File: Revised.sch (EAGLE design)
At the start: 17 parts, among them IC1 ATMEGA328P_PDIP

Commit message: Small tweaks
Remove capacitive coupling to RST#, which should enable debugWIRE
Thicken the power and ground traces, tweaking routes for clearance
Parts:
- removed C3: 0.1uF, SparkFun-Capacitors:CAP0402-CAP
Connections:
- removed net N$3: C3.2, IC1.PC6(/RESET), R1.1
- net RTS#: now also IC1.PC6(/RESET), R1.1; no longer C3.1
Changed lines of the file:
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@@
 <class number="0" name="default" width="0" drill="0">
 </class>
-<class number="1" name="power" width="0.6096" drill="0">
+<class number="1" name="power" width="0.8128" drill="0">
 </class>
 </classes>
@@
 <part name="R_TX" library="rcl" deviceset="R-US_" device="R0805" value="1k"/>
 <part name="R_RX" library="rcl" deviceset="R-US_" device="R0805" value="1k"/>
-<part name="C3" library="SparkFun-Capacitors" deviceset="CAP" device="0402-CAP" value="0.1uF"/>
 <part name="C1" library="rcl" deviceset="CPOL-US" device="E2,5-6E" value="47uF"/>
 <part name="JP1" library="jumper" deviceset="JP2E" device=""/>
@@
 <instance part="R_TX" gate="G$1" x="22.86" y="53.34"/>
 <instance part="R_RX" gate="G$1" x="22.86" y="60.96"/>
-<instance part="C3" gate="G$1" x="53.34" y="91.44" rot="R180"/>
 <instance part="C1" gate="G$1" x="2.54" y="101.6"/>
 <instance part="JP1" gate="1" x="20.32" y="91.44" rot="R180"/>
@@
 </segment>
 </net>
-<net name="N$3" class="0">
-<segment>
-<pinref part="C3" gate="G$1" pin="2"/>
-<wire x1="53.34" y1="99.06" x2="53.34" y2="93.98" width="0.1524" layer="91"/>
-<wire x1="53.34" y1="99.06" x2="58.42" y2="99.06" width="0.1524" layer="91"/>
-<label x="53.34" y="99.06" size="1.778" layer="95"/>
-<pinref part="R1" gate="G$1" pin="1"/>
-<wire x1="48.26" y1="99.06" x2="53.34" y2="99.06" width="0.1524" layer="91"/>
-<junction x="53.34" y="99.06"/>
-</segment>
-<segment>
-<pinref part="IC1" gate="G$1" pin="PC6(/RESET)"/>
-<wire x1="86.36" y1="93.98" x2="76.2" y2="93.98" width="0.1524" layer="91"/>
-<label x="76.2" y="93.98" size="1.778" layer="95"/>
-</segment>
-</net>
 <net name="TXD" class="0">
 <segment>
@@
 </segment>
 <segment>
-<pinref part="C3" gate="G$1" pin="1"/>
-<wire x1="53.34" y1="86.36" x2="53.34" y2="73.66" width="0.1524" layer="91"/>
-<label x="53.34" y="73.66" size="1.778" layer="95" rot="R90"/>
-</segment>
-</net>
+<label x="53.34" y="99.06" size="1.778" layer="95"/>
+<pinref part="R1" gate="G$1" pin="1"/>
+<wire x1="48.26" y1="99.06" x2="58.42" y2="99.06" width="0.1524" layer="91"/>
+</segment>
+<segment>
+<pinref part="IC1" gate="G$1" pin="PC6(/RESET)"/>
+<wire x1="86.36" y1="93.98" x2="76.2" y2="93.98" width="0.1524" layer="91"/>
+<label x="76.2" y="93.98" size="1.778" layer="95"/>
+</segment>
+</net>

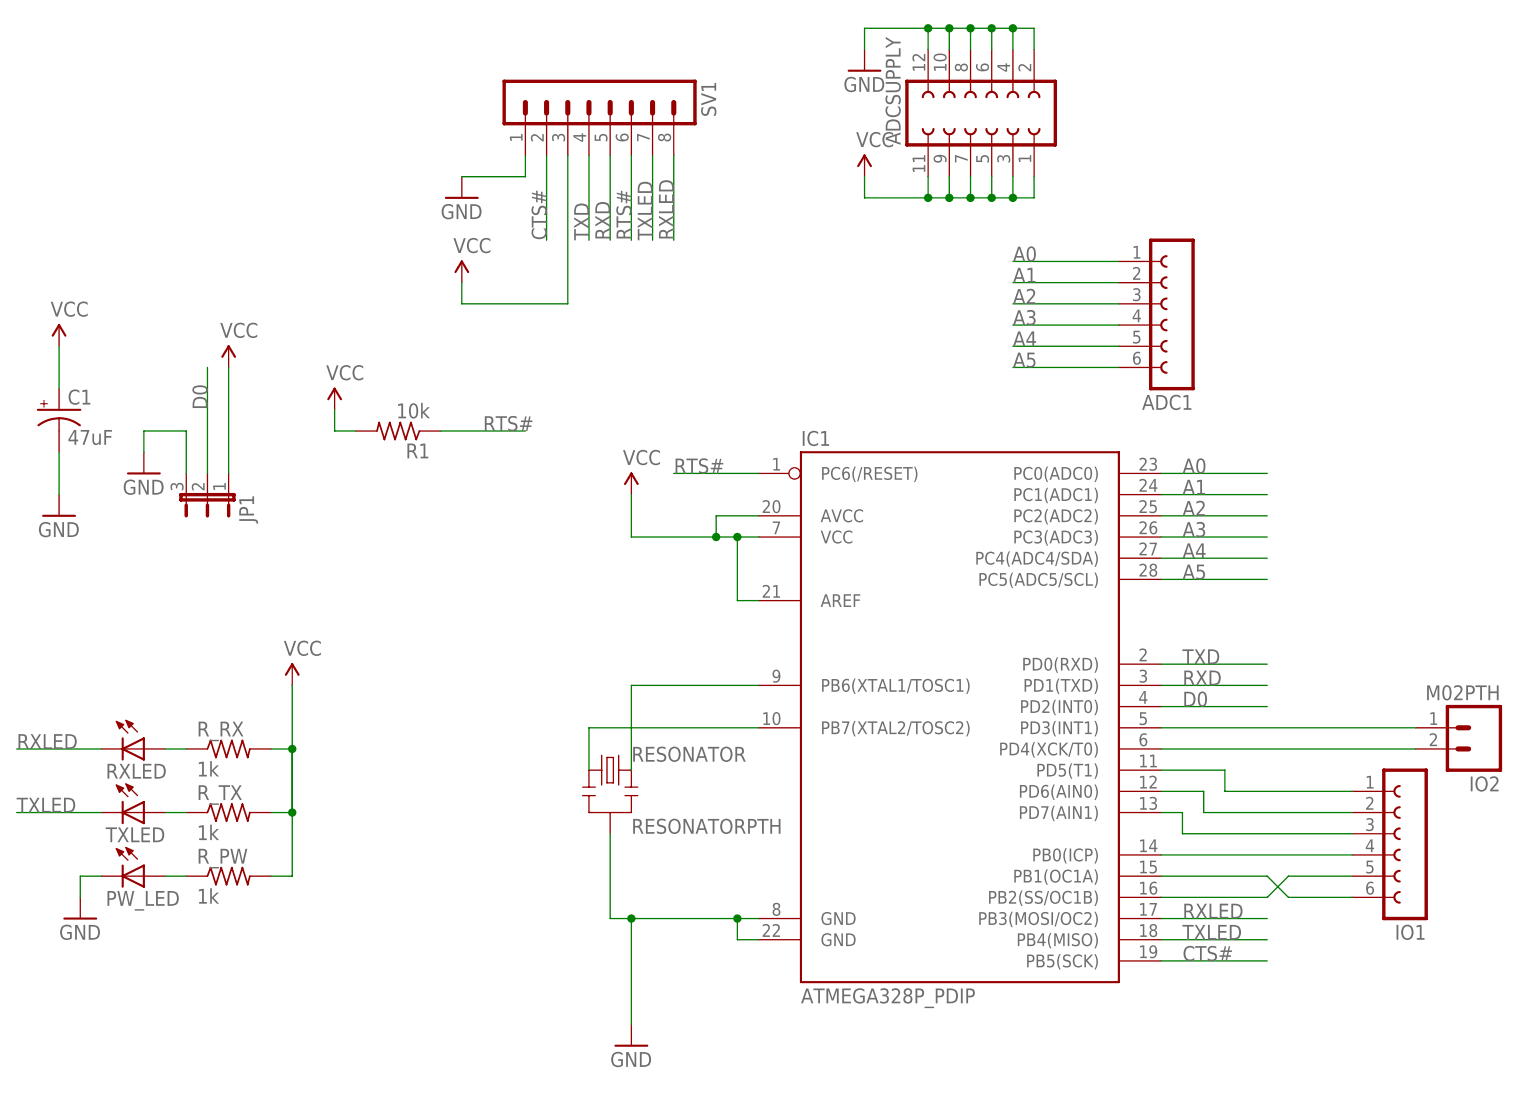
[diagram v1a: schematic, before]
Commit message: Cleanup
Change IO2 header pinouts to include the entire SPI bus
Move LEDs to PD5 (T1) and PB0 (ICP)
Move PB1 (OC1A) to CTS# connector
Redo some traces to avoid vias
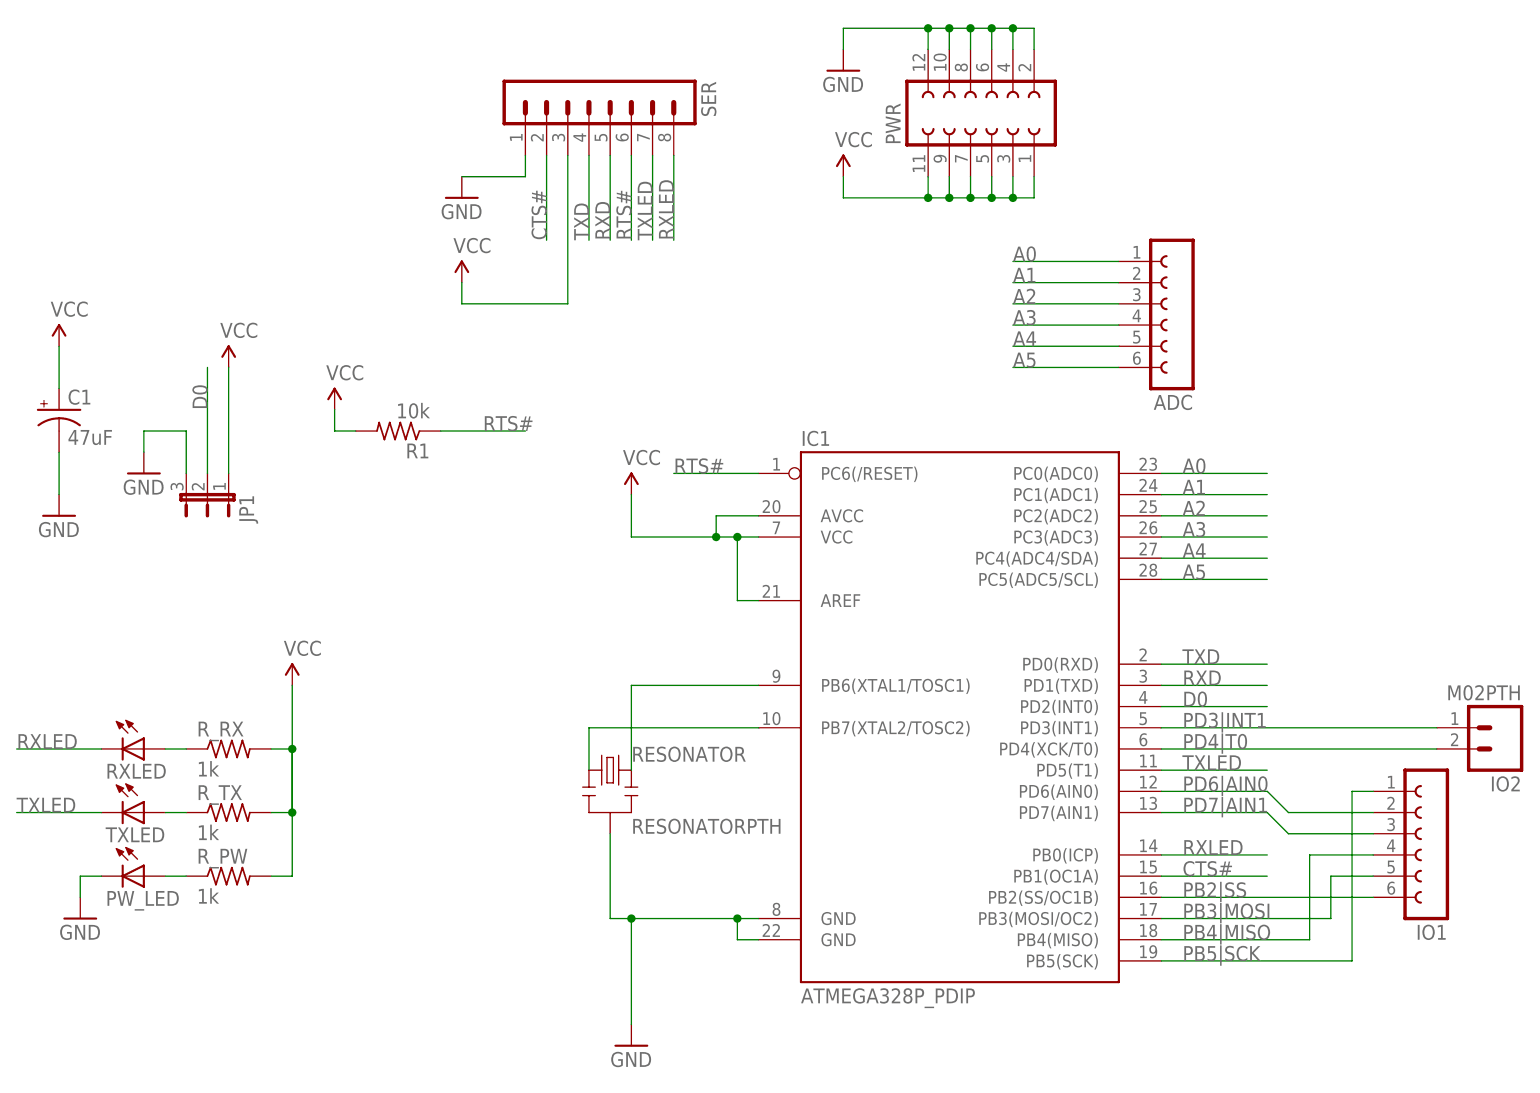
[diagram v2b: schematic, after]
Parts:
- renumbered ADC1 to ADC, ADCSUPPLY to PWR, SV1 to SER
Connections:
- net N$10 renamed PD6|AIN0
- net N$11 renamed PD7|AIN1
- net N$7 renamed PD3|INT1
- net N$8 renamed PD4|T0
- net POWER renamed VCC
- removed net N$12: IC1.PB0(ICP), IO1.4
- removed net N$13: IC1.PB1(OC1A), IO1.6
- removed net N$14: IC1.PB2(SS/OC1B), IO1.5
- removed net N$9: IC1.PD5(T1), IO1.1
- new net PB2|SS: IC1.PB2(SS/OC1B), IO1.6
- new net PB3|MOSI: IC1.PB3(MOSI/OC2), IO1.5
- new net PB4|MISO: IC1.PB4(MISO), IO1.4
- new net PB5|SCK: IC1.PB5(SCK), IO1.1
- net CTS#: now also IC1.PB1(OC1A); no longer IC1.PB5(SCK)
- net RXLED: now also IC1.PB0(ICP); no longer IC1.PB3(MOSI/OC2)
- net TXLED: now also IC1.PD5(T1); no longer IC1.PB4(MISO)
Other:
- moved on the sheet: IO1, IO2

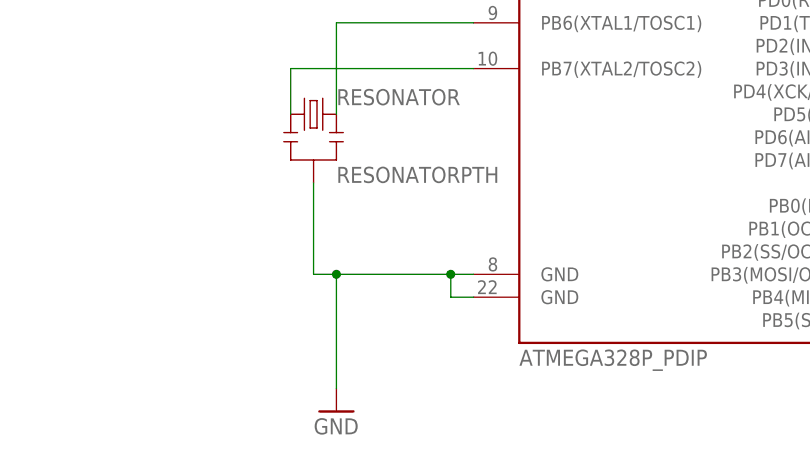
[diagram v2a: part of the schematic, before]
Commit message: Ground plane, better analog pin routing?
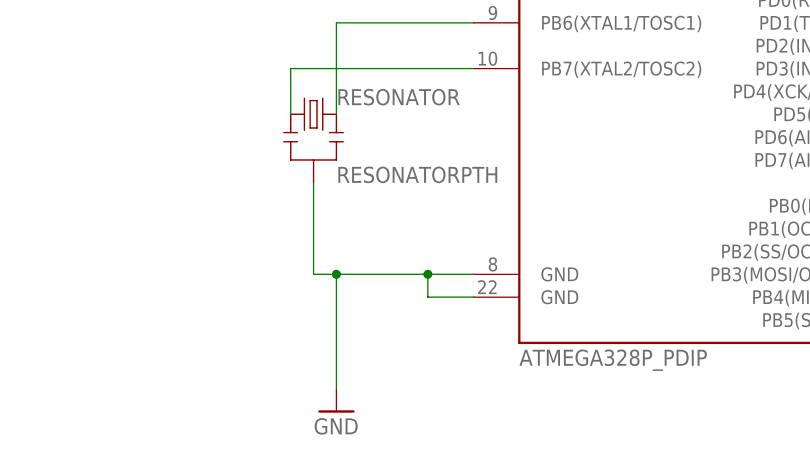
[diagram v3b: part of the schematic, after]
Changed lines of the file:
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@@
 <class number="1" name="power" width="0.8128" drill="0">
+</class>
+<class number="2" name="gnd" width="0.4064" drill="0">
 </class>
 </classes>
@@
 </busses>
 <nets>
-<net name="GND" class="1">
+<net name="GND" class="2">
 <segment>
 <pinref part="PWR" gate="G$1" pin="2"/>
@@
 <segment>
 <pinref part="IC1" gate="G$1" pin="GND@1"/>
-<wire x1="86.36" y1="40.64" x2="83.82" y2="40.64" width="0.1524" layer="91"/>
-<wire x1="83.82" y1="40.64" x2="71.12" y2="40.64" width="0.1524" layer="91"/>
+<wire x1="86.36" y1="40.64" x2="81.28" y2="40.64" width="0.1524" layer="91"/>
+<wire x1="81.28" y1="40.64" x2="71.12" y2="40.64" width="0.1524" layer="91"/>
 <wire x1="71.12" y1="40.64" x2="71.12" y2="27.94" width="0.1524" layer="91"/>
 <pinref part="GND4" gate="1" pin="GND"/>
@@
 <junction x="71.12" y="40.64"/>
 <pinref part="IC1" gate="G$1" pin="GND@2"/>
-<wire x1="86.36" y1="38.1" x2="83.82" y2="38.1" width="0.1524" layer="91"/>
-<wire x1="83.82" y1="38.1" x2="83.82" y2="40.64" width="0.1524" layer="91"/>
-<junction x="83.82" y="40.64"/>
+<wire x1="86.36" y1="38.1" x2="81.28" y2="38.1" width="0.1524" layer="91"/>
+<wire x1="81.28" y1="38.1" x2="81.28" y2="40.64" width="0.1524" layer="91"/>
+<junction x="81.28" y="40.64"/>
 </segment>
 <segment>
